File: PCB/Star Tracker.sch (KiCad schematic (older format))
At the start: 33 parts, among them J1 Conn_ARM_JTAG_SWD_10, U1 NCV565D2TG-ND, U2 DRV8833PW, U3 ATSAMD21E18A-AU, U4 AP7312-1833W6-7

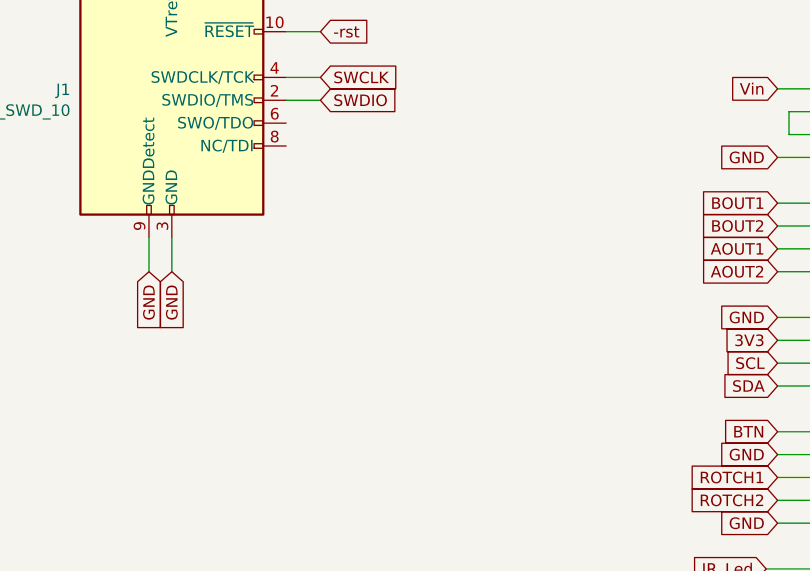
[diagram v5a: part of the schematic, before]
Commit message: Finished layout and greated gerbers. Off to fab!
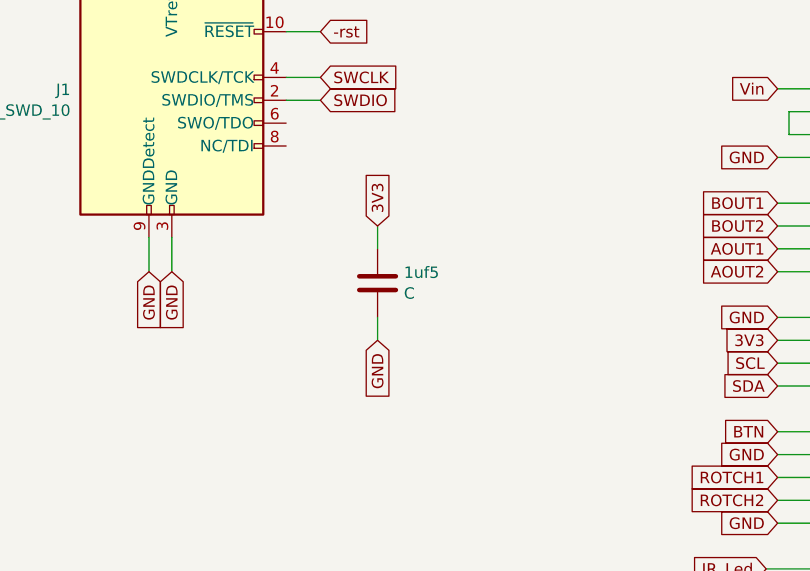
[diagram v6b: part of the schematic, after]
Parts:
- added 1uf5: C, Capacitor_SMD:C_1206_3216Metric_Pad1.42x1.75mm_HandSolder, symbol Device:C
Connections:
- net 3V3: now also 1uf5.1
- net GND: now also 1uf5.2
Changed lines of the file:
@@
 Wire Wire Line
 	3350 1500 3100 1500
+$Comp
+L Device:C 1uf5
+U 1 1 5DA3F7E8
+P 7800 2450
+F 0 "1uf5" H 7915 2496 50  0000 L CNN
+F 1 "C" H 7915 2405 50  0000 L CNN
+F 2 "Capacitor_SMD:C_1206_3216Metric_Pad1.42x1.75mm_HandSolder" H 7838 2300 50  0001 C CNN
+F 3 "~" H 7800 2450 50  0001 C CNN
+	1    7800 2450
+	1    0    0    -1
+$EndComp
+Text GLabel 7800 2200 1    50   Input ~ 0
+3V3
+Text GLabel 7800 2700 3    50   Input ~ 0
+GND
+Wire Wire Line
+	7800 2200 7800 2300
+Wire Wire Line
+	7800 2600 7800 2700
 $EndSCHEMATC

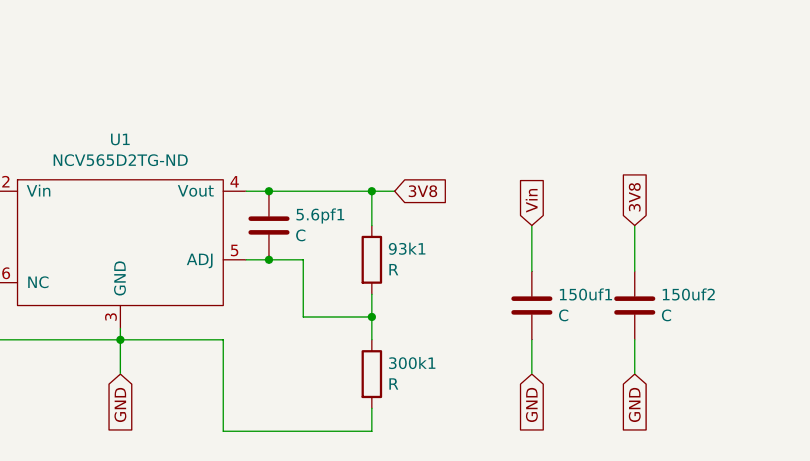
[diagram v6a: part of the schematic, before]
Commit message: Swapped 93k and 300k resistors
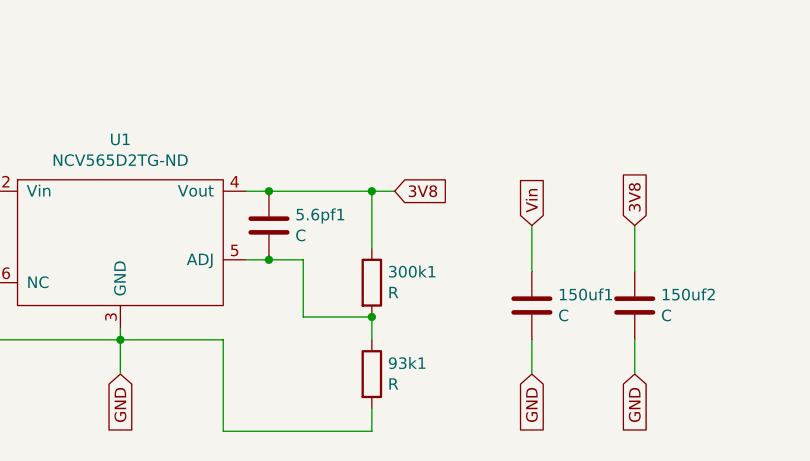
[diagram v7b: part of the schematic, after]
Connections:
- net 3V8: now also 300k1.1; no longer 93k1.1
- net GND: now also 93k1.2; no longer 300k1.2
- net at 5.6pf1.2, U1.5 (ADJ): now also 300k1.2, 93k1.1; no longer 300k1.1, 93k1.2
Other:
- moved on the sheet: 300k1, 93k1
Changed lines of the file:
@@
 L Device:R 93k1
 U 1 1 5D8C118C
-P 2700 6600
-F 0 "93k1" H 2770 6646 50  0000 L CNN
-F 1 "R" H 2770 6555 50  0000 L CNN
-F 2 "Resistor_SMD:R_1206_3216Metric_Pad1.42x1.75mm_HandSolder" V 2630 6600 50  0001 C CNN
-F 3 "~" H 2700 6600 50  0001 C CNN
-	1    2700 6600
-	1    0    0    -1
-$EndComp
-$Comp
-L Device:R 300k1
-U 1 1 5D8C16CD
 P 2700 7100
-F 0 "300k1" H 2770 7146 50  0000 L CNN
+F 0 "93k1" H 2770 7146 50  0000 L CNN
 F 1 "R" H 2770 7055 50  0000 L CNN
 F 2 "Resistor_SMD:R_1206_3216Metric_Pad1.42x1.75mm_HandSolder" V 2630 7100 50  0001 C CNN
@@
 	1    0    0    -1
 $EndComp
-Wire Wire Line
-	2700 6450 2700 6300
+$Comp
+L Device:R 300k1
+U 1 1 5D8C16CD
+P 2700 6700
+F 0 "300k1" H 2770 6746 50  0000 L CNN
+F 1 "R" H 2770 6655 50  0000 L CNN
+F 2 "Resistor_SMD:R_1206_3216Metric_Pad1.42x1.75mm_HandSolder" V 2630 6700 50  0001 C CNN
+F 3 "~" H 2700 6700 50  0001 C CNN
+	1    2700 6700
+	1    0    0    -1
+$EndComp
 Connection ~ 2700 6300
 Wire Wire Line
 	2700 6300 2800 6300
 Wire Wire Line
-	2700 6750 2700 6850
+	2700 7250 2700 7350
 Wire Wire Line
 	2150 6600 2250 6600
@@
 Wire Wire Line
 	2400 6850 2700 6850
-Connection ~ 2700 6850
 Wire Wire Line
 	2700 6850 2700 6950
-Wire Wire Line
-	2700 7250 2700 7350
 Wire Wire Line
 	2700 7350 2050 7350
@@
 Wire Wire Line
 	7800 2600 7800 2700
+Connection ~ 2700 6850
+Wire Wire Line
+	2700 6300 2700 6550
 $EndSCHEMATC
